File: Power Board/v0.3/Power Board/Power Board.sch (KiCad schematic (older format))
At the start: 6 parts, among them J1 Battery In, J2 Conn_01x06, SW1 SW_Push

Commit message: Create the LED panel supply circuit.
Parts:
- added D2: LED, blue, LED_SMD:LED_0603_1608Metric, symbol Device:LED
- added F1, F2, F3, F4, F5, F6: Fuse, Fuse:Fuse_1206_3216Metric, symbol Device:Fuse
- added J2, J3, J4, J5, J6, J7: JST B2PS-VH, Connector_JST:JST_VH_B2PS-VH_1x02_P3.96mm_Horizontal, symbol Connector_Generic:Conn_01x02
- added R2: 680, Resistor_SMD:R_0603_1608Metric_Pad1.05x0.95mm_HandSolder, symbol Device:R
- J1: footprint xxxx -> ~
- J8: renamed from J2; symbol Connector_Generic:Conn_01x06 -> Connector_Generic:Conn_01x07
- R1: renamed from R?; footprint Resistor_SMD:R_0603_1608Metric -> Resistor_SMD:R_0603_1608Metric_Pad1.05x0.95mm_HandSolder
- gave numbers to parts that had none: 2
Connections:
- net labels added: 5.2V_switched, Battery_Power, Panel_Alert, Panel_Power
- wire segments 31 -> 69
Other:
- note added: "Power Board"
- moved on the sheet: D1, J1, L1, R1, SW1

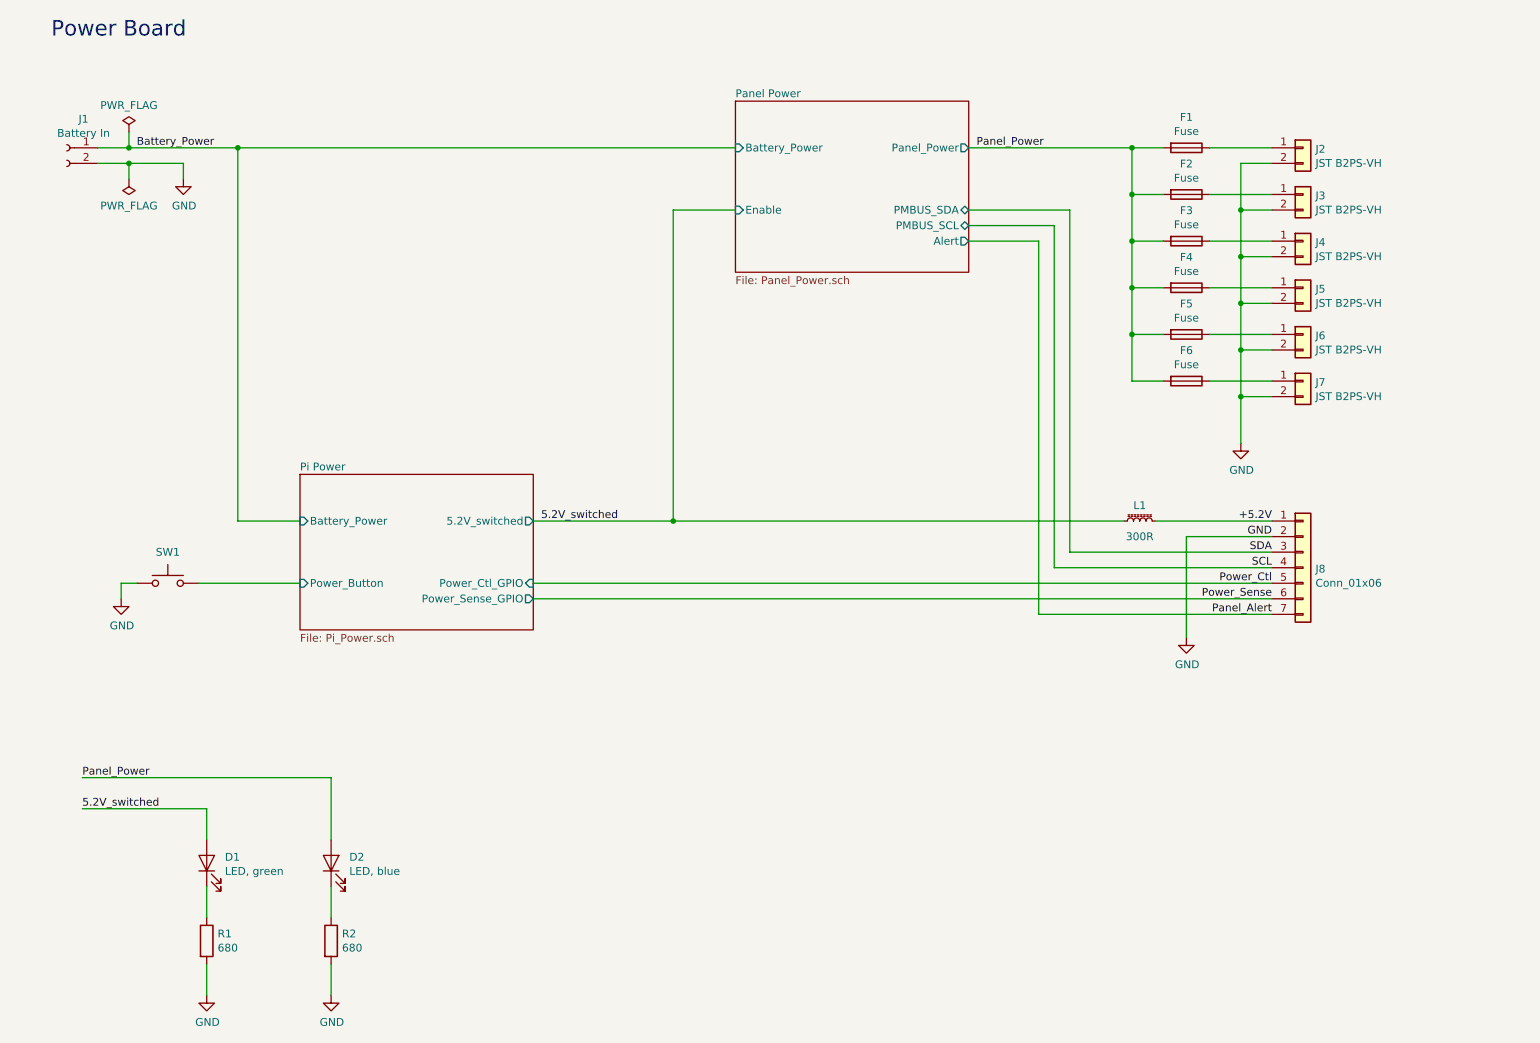
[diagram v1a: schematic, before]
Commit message: Update components with available parts.
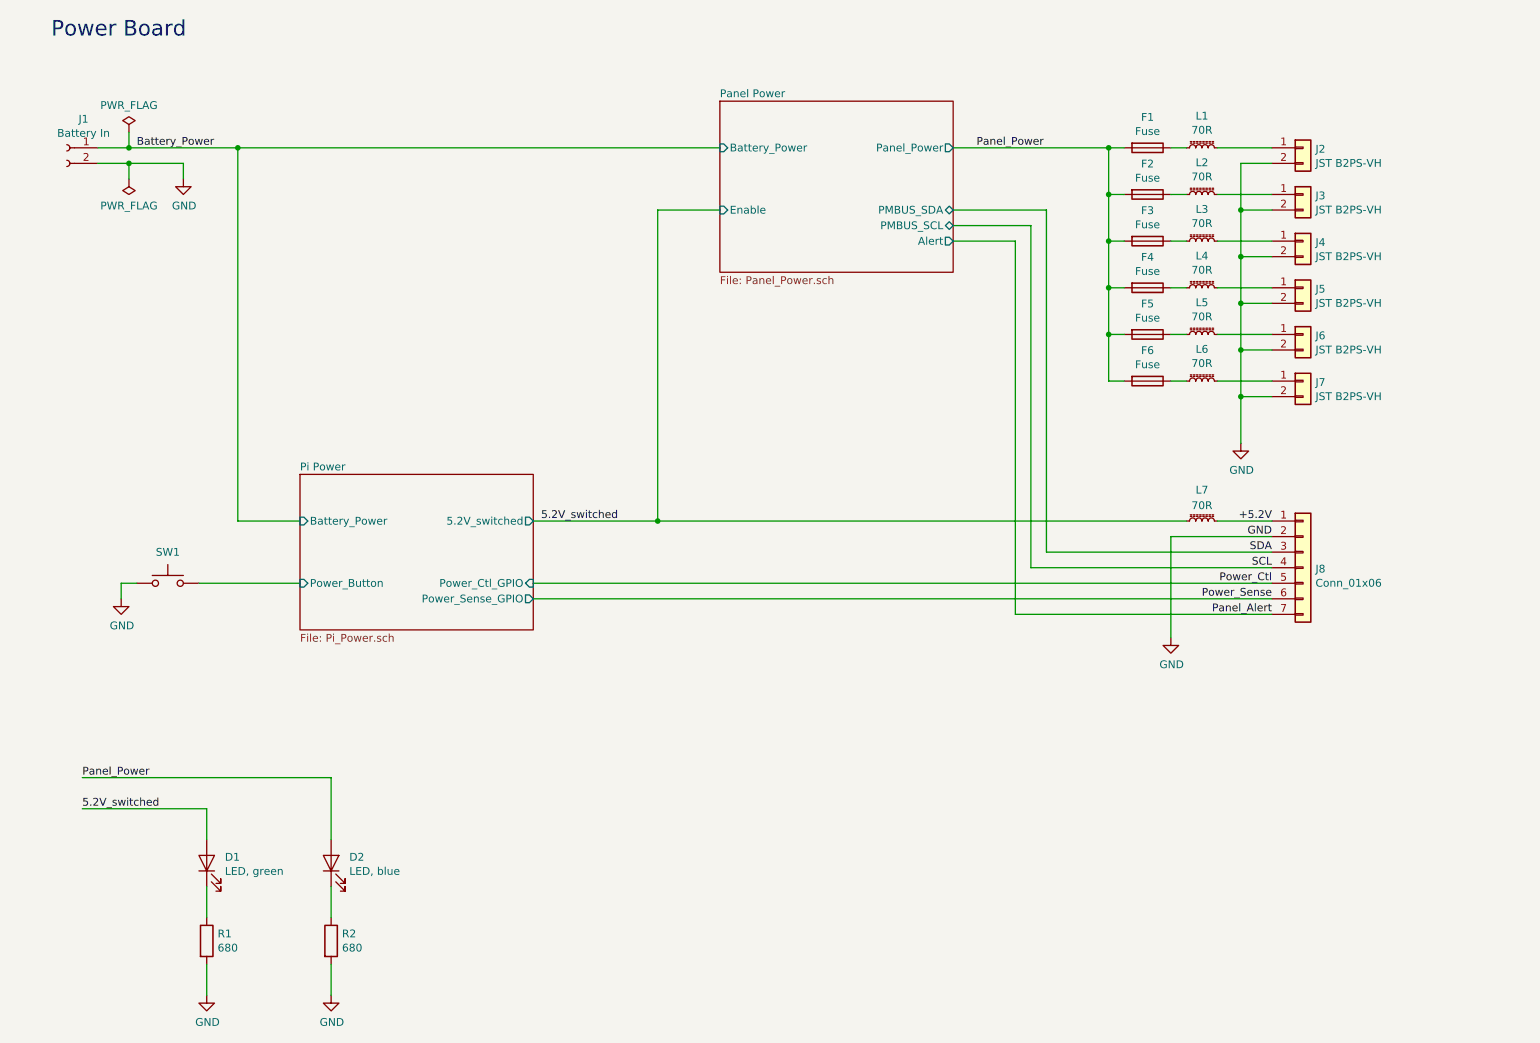
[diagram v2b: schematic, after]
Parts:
- added L1, L2, L3, L4, L5, L6: 70R, Inductor_SMD:L_0603_1608Metric, symbol Device:L_Core_Ferrite_Small
- D1, D2, R1, R2: Digikey No. (none) -> -
- L7: renamed from L1; value 300R -> 70R; Digikey No. not avail. -> 490-5224-1-ND; Manufacturer NIC -> Murata; Part No. NCB-H0603R301TR100F -> BLM18SG700TN1D
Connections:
- net at J2.1 (Pin_1): now also L1.2; no longer F1.1
- net at J3.1 (Pin_1): now also L2.2; no longer F2.1
- net at J4.1 (Pin_1): now also L3.2; no longer F3.1
- net at J5.1 (Pin_1): now also L4.2; no longer F4.1
- net at J6.1 (Pin_1): now also L5.2; no longer F5.1
- net at J7.1 (Pin_1): now also L6.2; no longer F6.1
- new net: F1.1, L1.1
- new net: F2.1, L2.1
- new net: F3.1, L3.1
- new net: F4.1, L4.1
- new net: F5.1, L5.1
- new net: F6.1, L6.1
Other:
- moved on the sheet: F1, F2, F3, F4, F5, F6, L7

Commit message: Draw all custom footprints and assign to components.
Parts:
- J1: footprint ~ -> Power_Board:Molex_Microfit_43650-0203
- J8: value Conn_01x06 -> Molex 70553-0005; footprint (none) -> Power_Board:Molex_SL_70553-0005
- SW1: footprint (none) -> Power_Board:PTS645-Vx-39-2

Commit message: Work in progress.
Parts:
- J8: value Molex 70553-0005 -> Molex 70553-0006; footprint Power_Board:Molex_SL_70553-0005 -> Power_Board:Molex_SL_70553-0006
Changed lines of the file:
@@
 P 9050 4600
 F 0 "J8" H 9130 4592 50  0000 L CNN
-F 1 "Molex 70553-0005" H 9130 4501 50  0000 L CNN
-F 2 "Power_Board:Molex_SL_70553-0005" H 9050 4600 50  0001 C CNN
+F 1 "Molex 70553-0006" H 9130 4501 50  0000 L CNN
+F 2 "Power_Board:Molex_SL_70553-0006" H 9050 4600 50  0001 C CNN
 F 3 "~" H 9050 4600 50  0001 C CNN
 F 4 "WM4904-ND" H -750 350 50  0001 C CNN "Digikey No."

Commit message: Work in progress.
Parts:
- J1: footprint Power_Board:Molex_Microfit_43650-0203 -> Connector_JST:JST_VH_B3PS-VH_1x03_P3.96mm_Horizontal; symbol Connector:Conn_01x02_Female -> Connector:Conn_01x03_Male
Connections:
- net GND: now also J1.3 (Pin_3); no longer J1.2 (Pin_2)
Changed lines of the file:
@@
 L power:PWR_FLAG #FLG02
 U 1 1 5C9A6A29
-P 1500 2100
-F 0 "#FLG02" H 1500 2175 50  0001 C CNN
-F 1 "PWR_FLAG" H 1500 2273 50  0000 C CNN
-F 2 "" H 1500 2100 50  0001 C CNN
-F 3 "~" H 1500 2100 50  0001 C CNN
-	1    1500 2100
+P 1500 2200
+F 0 "#FLG02" H 1500 2275 50  0001 C CNN
+F 1 "PWR_FLAG" H 1500 2373 50  0000 C CNN
+F 2 "" H 1500 2200 50  0001 C CNN
+F 3 "~" H 1500 2200 50  0001 C CNN
+	1    1500 2200
 	-1   0    0    1
 $EndComp
 Wire Wire Line
-	1300 2000 1500 2000
-Wire Wire Line
-	1500 2000 1500 2100
+	1300 2100 1500 2100
+Wire Wire Line
+	1500 2100 1500 2200
 Wire Wire Line
 	1300 1900 1500 1900
@@
 	1500 1900 1500 1800
 Wire Wire Line
-	1500 2000 1850 2000
-Wire Wire Line
-	1850 2000 1850 2100
-Connection ~ 1500 2000
+	1500 2100 1850 2100
+Wire Wire Line
+	1850 2100 1850 2200
+Connection ~ 1500 2100
 $Comp
 L power:GND #PWR02
 U 1 1 5C9A724E
-P 1850 2100
-F 0 "#PWR02" H 1850 1850 50  0001 C CNN
-F 1 "GND" H 1855 1927 50  0000 C CNN
-F 2 "" H 1850 2100 50  0001 C CNN
-F 3 "" H 1850 2100 50  0001 C CNN
-	1    1850 2100
+P 1850 2200
+F 0 "#PWR02" H 1850 1950 50  0001 C CNN
+F 1 "GND" H 1855 2027 50  0000 C CNN
+F 2 "" H 1850 2200 50  0001 C CNN
+F 3 "" H 1850 2200 50  0001 C CNN
+	1    1850 2200
 	1    0    0    -1
 $EndComp
@@
 $EndComp
 $Comp
-L Connector:Conn_01x02_Female J1
+L Connector:Conn_01x03_Male J1
 U 1 1 5C9104AD
-P 1100 1900
-F 0 "J1" H 992 2085 50  0000 C CNN
-F 1 "Battery In" H 992 1994 50  0000 C CNN
-F 2 "Power_Board:Molex_Microfit_43650-0203" H 1100 1900 50  0001 C CNN
-F 3 "https://www.molex.com/pdm_docs/sd/436500205_sd.pdf" H 1100 1900 50  0001 C CNN
-F 4 "WM17581-ND" H -650 -850 50  0001 C CNN "Digikey No."
-F 5 "Molex" H -650 -850 50  0001 C CNN "Manufacturer"
-F 6 "43650-0205" H -650 -850 50  0001 C CNN "Part No."
-	1    1100 1900
-	-1   0    0    -1
+P 1100 2000
+F 0 "J1" H 992 2185 50  0000 C CNN
+F 1 "Battery In" H 992 2094 50  0000 C CNN
+F 2 "Connector_JST:JST_VH_B3PS-VH_1x03_P3.96mm_Horizontal" H 1100 2000 50  0001 C CNN
+F 3 "https://www.molex.com/pdm_docs/sd/436500205_sd.pdf" H 1100 2000 50  0001 C CNN
+F 4 "WM17581-ND" H -650 -750 50  0001 C CNN "Digikey No."
+F 5 "Molex" H -650 -750 50  0001 C CNN "Manufacturer"
+F 6 "43650-0205" H -650 -750 50  0001 C CNN "Part No."
+	1    1100 2000
+	1    0    0    -1
 $EndComp
 $EndSCHEMATC
